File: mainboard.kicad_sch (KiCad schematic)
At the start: 29 parts, among them J1 terminal_led-strip, J2 header_rotary-encoder, J4 header_pi, J5 power_input, J6 AudioJack2, Q1 IRF9540N, SW1 power_switch, U1 OPA2277, U2 MSGEQ7, U4 logic-level-converter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

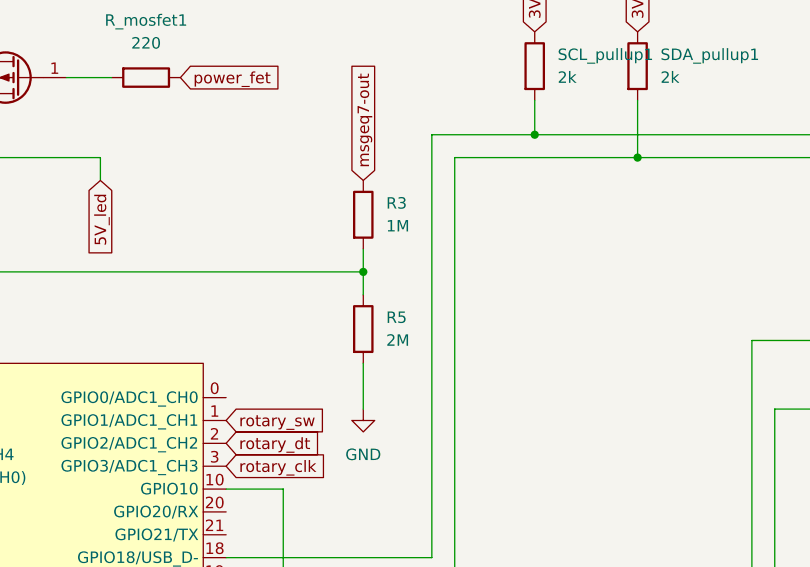
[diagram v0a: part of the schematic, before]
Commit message: add proper values for voltage divider of msgeq7-out
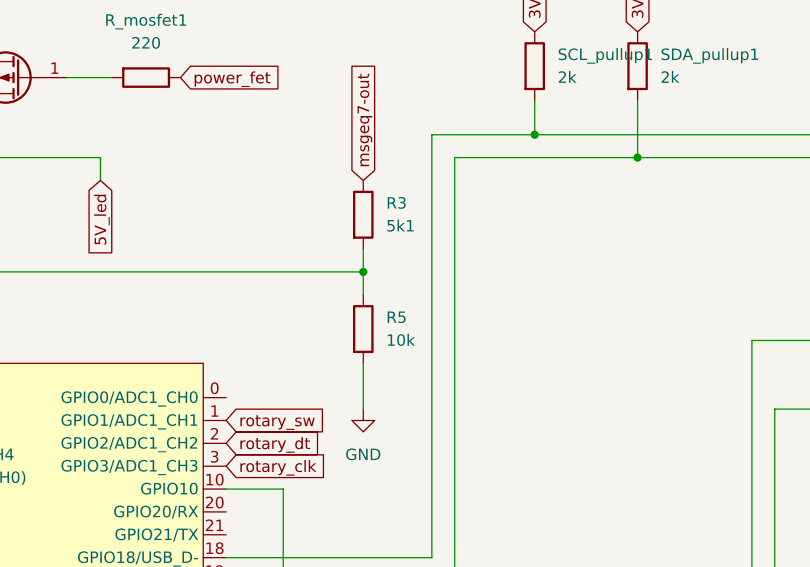
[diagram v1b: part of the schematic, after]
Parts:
- R3: value 1M -> 5k1; LCSC (none) -> C27834
- R5: value 2M -> 10k; LCSC (none) -> C17414
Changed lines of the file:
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@@
       (effects (font (size 1.27 1.27)) (justify left))
     )
-    (property "Value" "2M" (at 134.62 74.93 0)
+    (property "Value" "10k" (at 134.62 74.93 0)
       (effects (font (size 1.27 1.27)) (justify left))
     )
@@
       (effects (font (size 1.27 1.27)) hide)
     )
-    (property "LCSC" "" (at 132.08 73.66 0)
+    (property "LCSC" "C17414" (at 132.08 73.66 0)
       (effects (font (size 1.27 1.27)) hide)
     )
@@
       (effects (font (size 1.27 1.27)) (justify left))
     )
-    (property "Value" "1M" (at 134.62 62.23 0)
+    (property "Value" "5k1" (at 134.62 62.23 0)
       (effects (font (size 1.27 1.27)) (justify left))
     )
@@
       (effects (font (size 1.27 1.27)) hide)
     )
-    (property "LCSC" "" (at 132.08 60.96 0)
-      (effects (font (size 1.27 1.27)) hide)
-    )
+    (property "LCSC" "C27834" (at 132.08 60.96 0)
+      (effects (font (size 1.27 1.27)) hide)
+    )

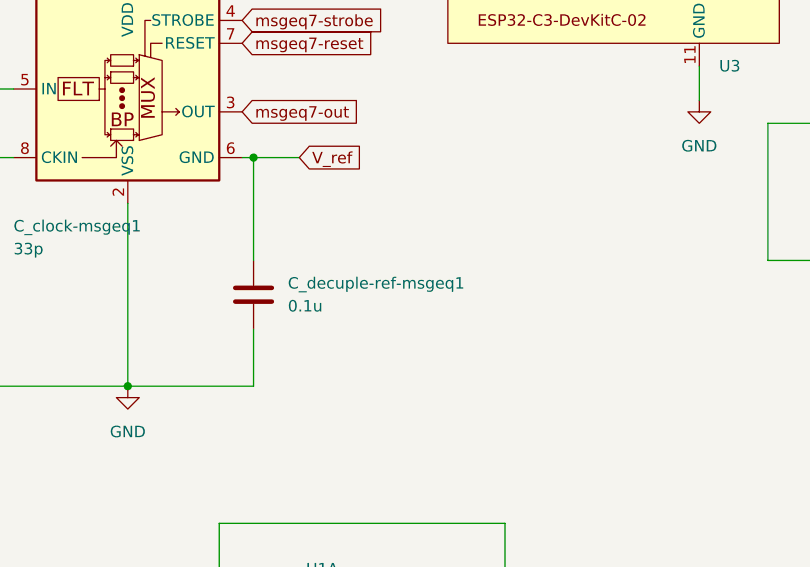
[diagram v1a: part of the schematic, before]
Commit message: ground mounting holes
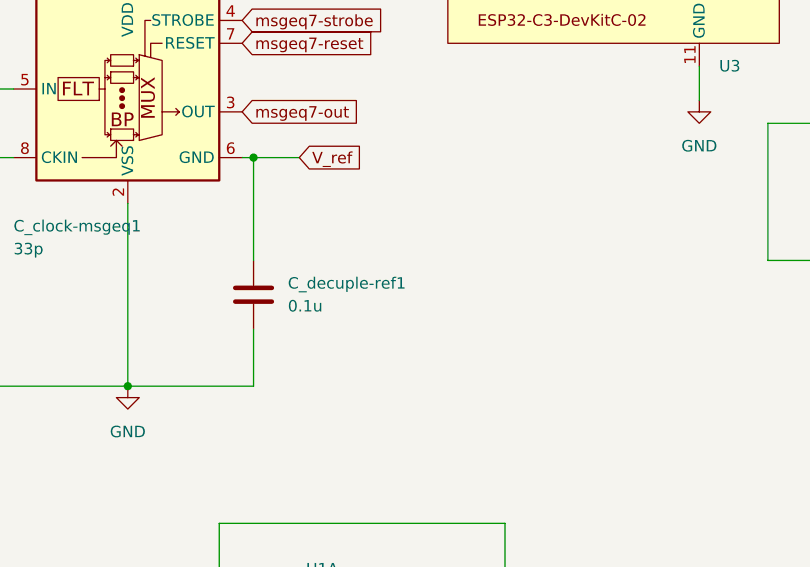
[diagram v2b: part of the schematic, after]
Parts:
- renumbered C_decuple-ref-msgeq1 to C_decuple-ref1
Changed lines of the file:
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@@
   (symbol (lib_id "Device:C") (at 55.88 135.89 0) (unit 1)
     (in_bom yes) (on_board yes) (dnp no) (fields_autoplaced)
-    (property "Reference" "C_decuple-ref-msgeq1" (at 59.69 134.62 0)
+    (property "Reference" "C_decuple-ref1" (at 59.69 134.62 0)
       (effects (font (size 1.27 1.27)) (justify left))
     )
@@
       (project "mainboard"
         (path "/3161c04b-751c-4104-8356-8b48a6ef4a37"
-          (reference "C_decuple-ref-msgeq1") (unit 1)
+          (reference "C_decuple-ref1") (unit 1)
         )
       )
